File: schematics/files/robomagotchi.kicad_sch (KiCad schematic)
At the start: 26 parts, among them M1 Servo Motor, U1 SPI TFT DISPLAY (ILI9341), U2 I2C OLED Display (SSD1306), U3 Ultrasonic Proximity Sensor (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, U4 Temp Sensor (DHT11), U5 IR Receiver (VS18838B)

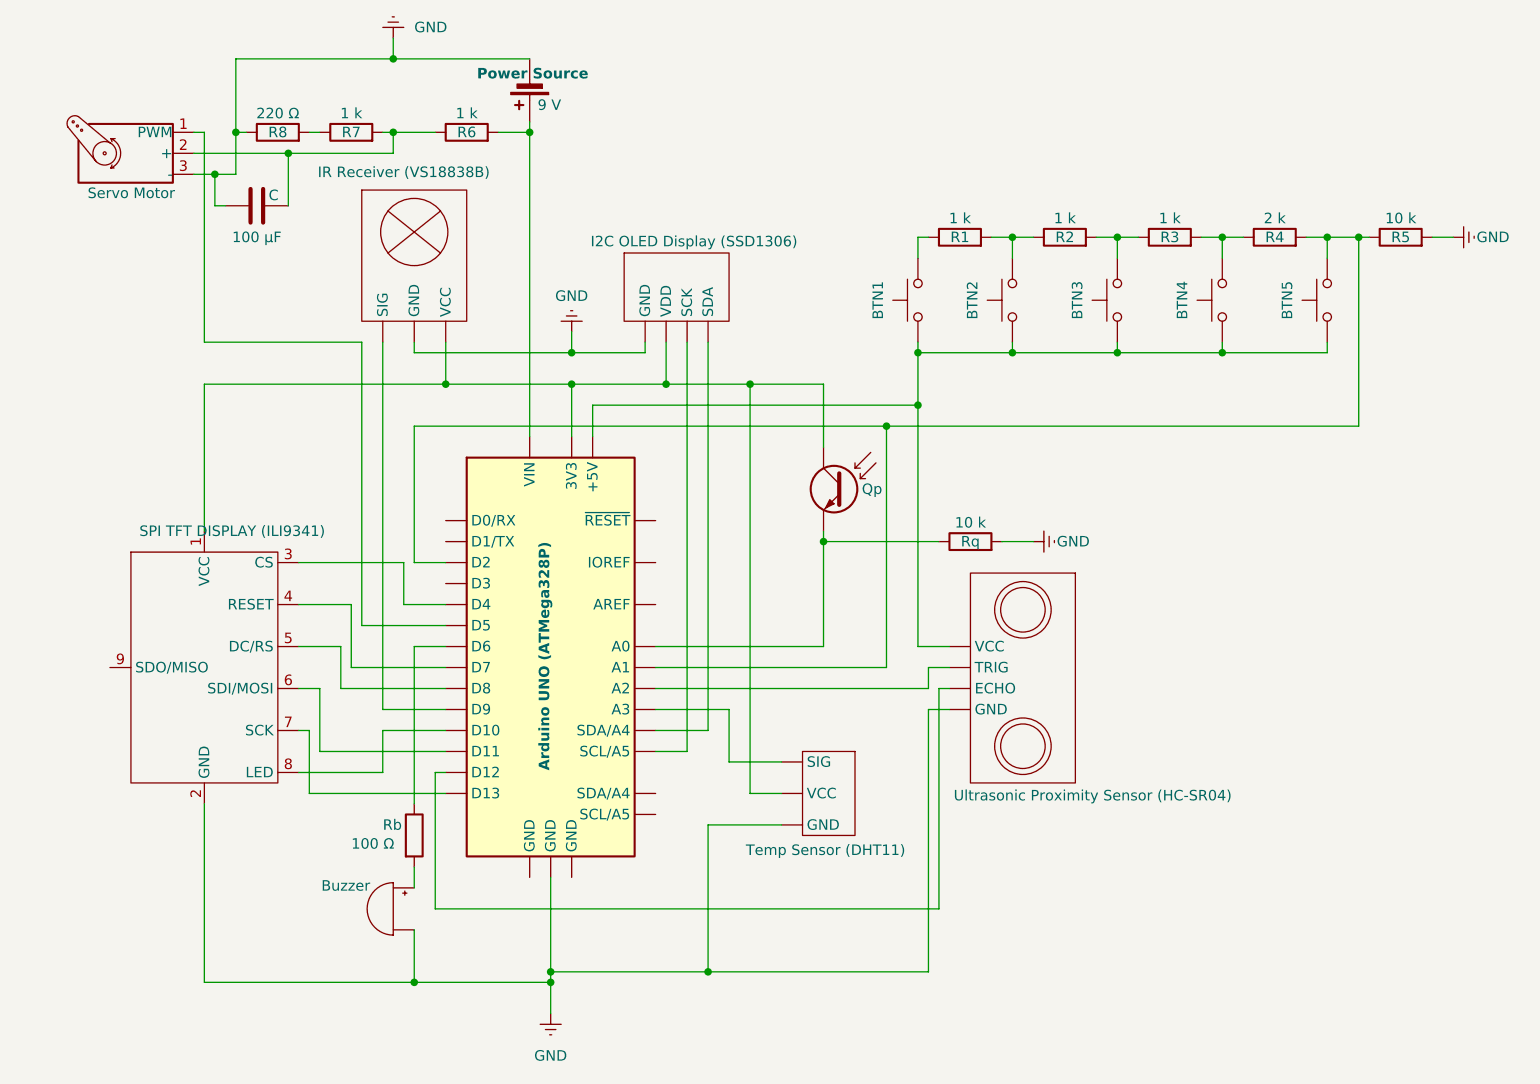
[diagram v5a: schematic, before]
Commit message: Replaced display. Changed resistor ladder.
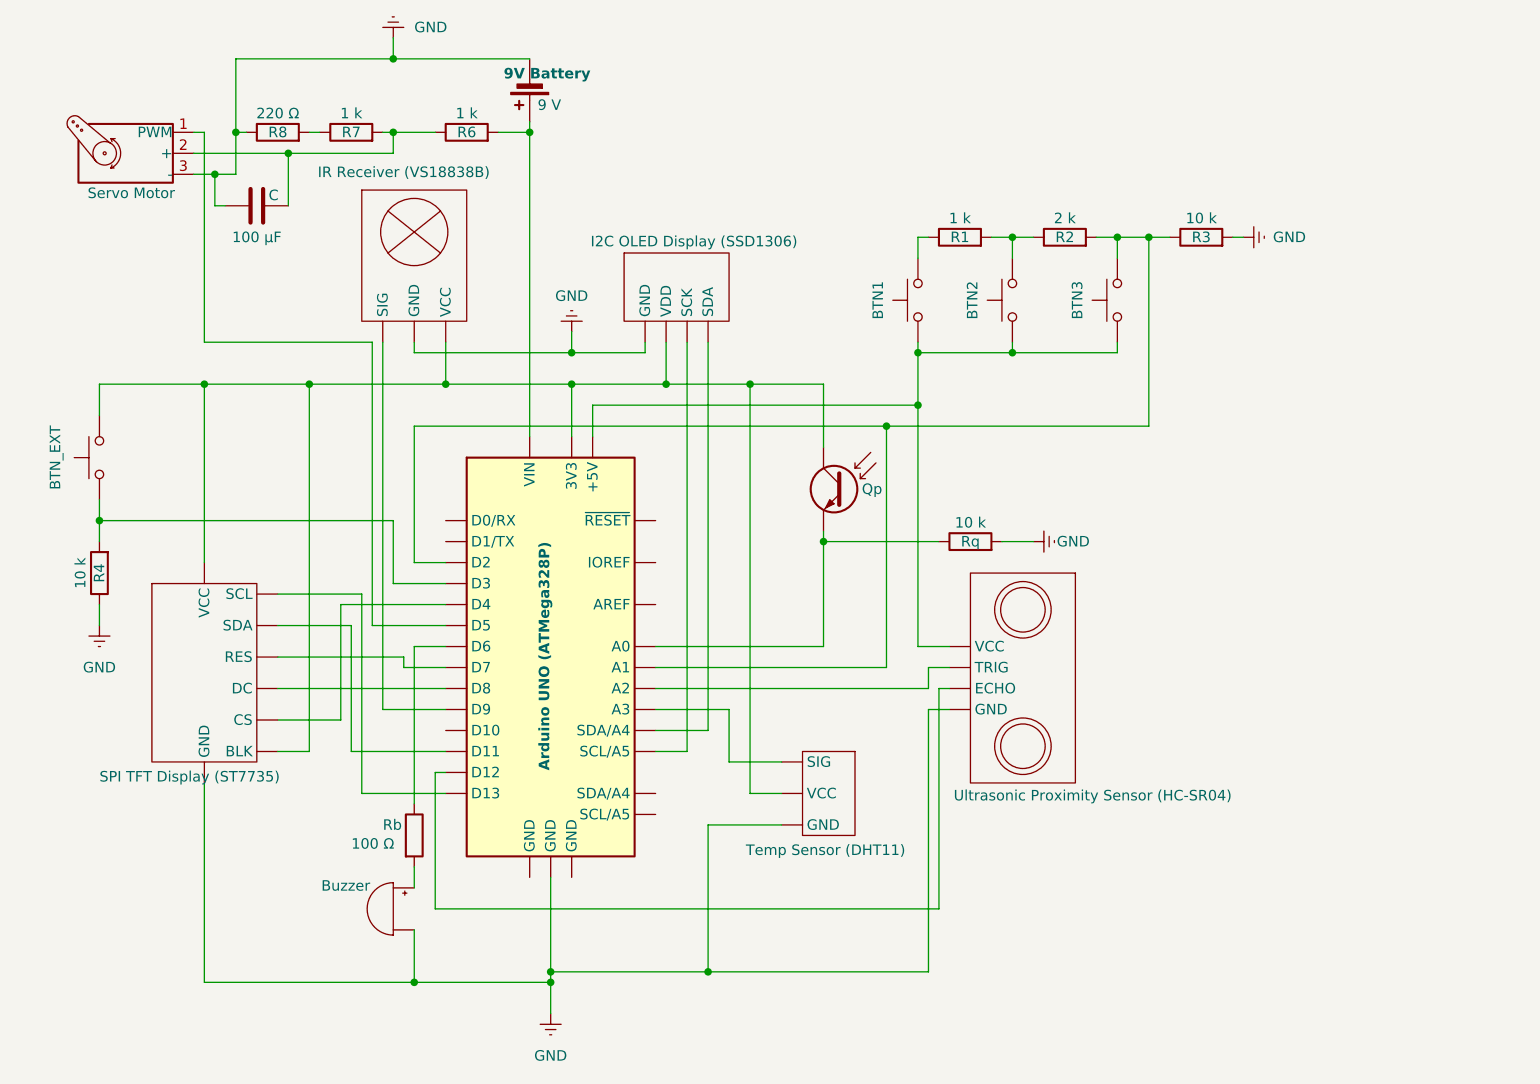
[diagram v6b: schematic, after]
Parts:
- removed BTN5: SW_Push, symbol Switch:SW_Push
- removed R3: 1 k, symbol Device:R
- removed U1: SPI TFT DISPLAY (ILI9341), symbol A_LAPTOP_LIB:ILI9341_SPI_TFT
- added U1: SPI TFT Display (ST7735), symbol A_LAPTOP_LIB:ST7735_SPI_TFT_Display
- R2: value 1 k -> 2 k
- R4: value 2 k -> 10 k
- renumbered BTN4 to BTN_EXT, R5 to R3
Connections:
- net GND: now also R4.1, U1.1 (GND)
- net at BTN3.2, R2.2: now also A2.10 (A1), A2.17 (D2), R3.1
- net at BTN_EXT.2: now also A2.4 (3V3), Qp.1 (C), U2. (VDD), U4. (VCC), U5. (VCC), U1.2 (VCC), U1.8 (BLK); no longer R4.1
- net at A2.5 (+5V), BTN1.1, BTN2.1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: no longer BTN_EXT.1
- net at A2.19 (D4): now also U1.7 (CS)
- net at A2.22 (D7): now also U1.5 (RES)
- net at A2.23 (D8): now also U1.6 (DC)
- net at A2.26 (D11): now also U1.4 (SDA)
- net at A2.28 (D13): now also U1.3 (SCL)
- net at A2.18 (D3): now also BTN_EXT.1, R4.2
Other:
- moved on the sheet: BTN_EXT, R3

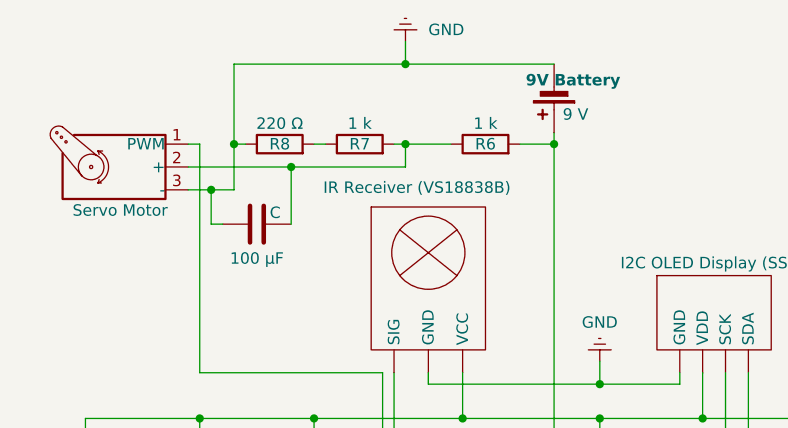
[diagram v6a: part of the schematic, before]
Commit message: Fixed resistor numerotation error.
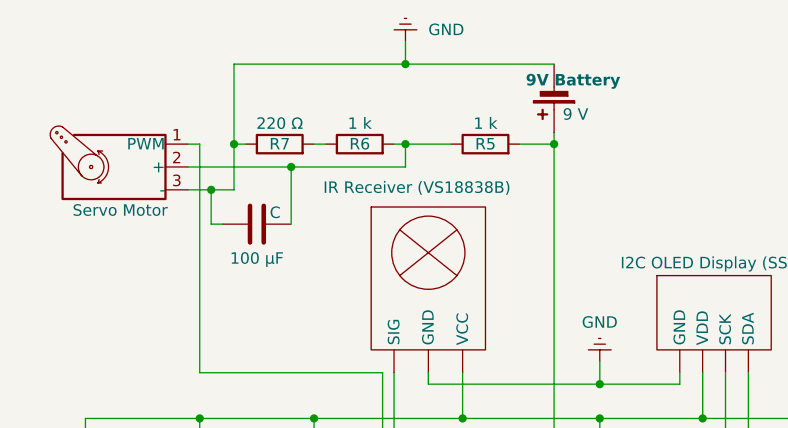
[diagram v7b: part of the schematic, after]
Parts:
- renumbered R6 to R5, R7 to R6, R8 to R7
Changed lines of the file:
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@@
 		(on_board yes)
 		(dnp no)
-		(property "Reference" "R6"
+		(property "Reference" "R5"
 			(at 120.65 44.45 90)
 			(effects
@@
 			(project "robomagotchi"
 				(path "/564f43e2-925d-4726-ad2e-2e1f480b3347"
-					(reference "R6")
+					(reference "R5")
 					(unit 1)
 				)
@@
 		(on_board yes)
 		(dnp no)
-		(property "Reference" "R7"
+		(property "Reference" "R6"
 			(at 106.68 44.45 90)
 			(effects
@@
 			(project "robomagotchi"
 				(path "/564f43e2-925d-4726-ad2e-2e1f480b3347"
-					(reference "R7")
+					(reference "R6")
 					(unit 1)
 				)
@@
 		(on_board yes)
 		(dnp no)
-		(property "Reference" "R8"
+		(property "Reference" "R7"
 			(at 97.79 44.45 90)
 			(effects
@@
 			(project "robomagotchi"
 				(path "/564f43e2-925d-4726-ad2e-2e1f480b3347"
-					(reference "R8")
-					(unit 1)
-				)
+					(reference "R7")
+					(unit 1)
+				)

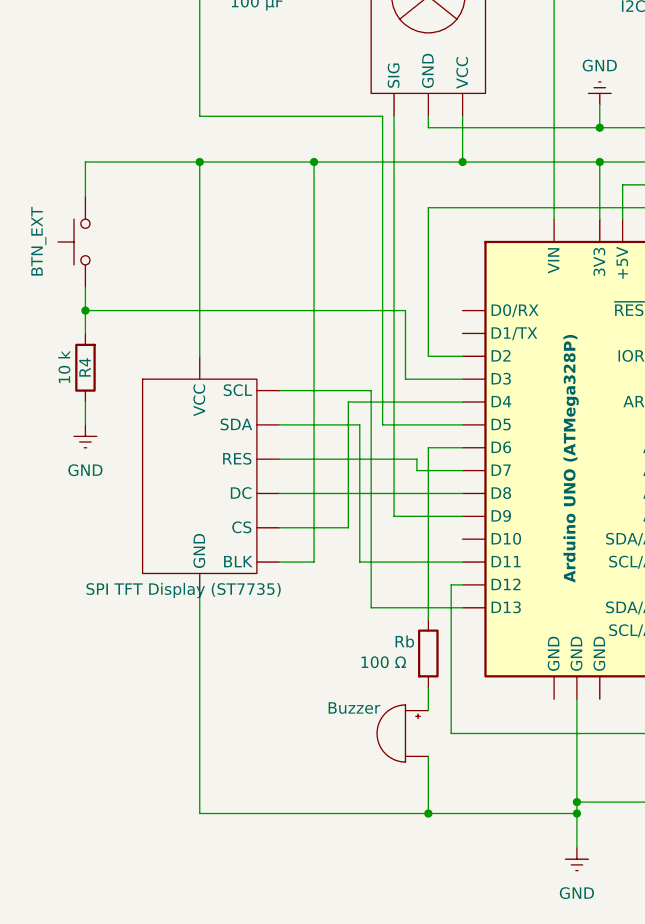
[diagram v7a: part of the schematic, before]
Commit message: Added init funcs for most components
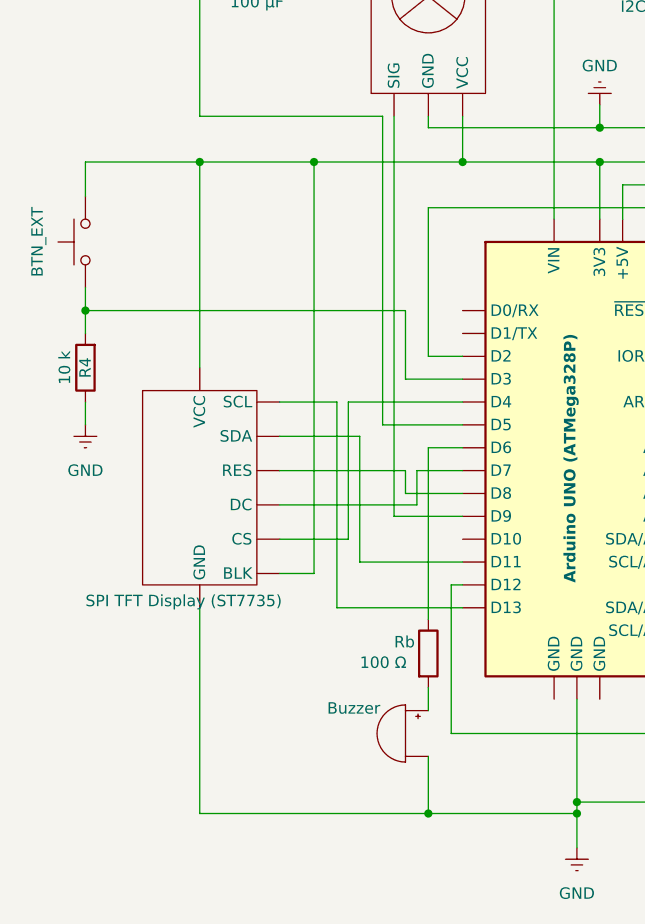
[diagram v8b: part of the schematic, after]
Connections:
- net at U1.5 (RES): now also A2.23 (D8); no longer A2.22 (D7)
- net at U1.6 (DC): now also A2.22 (D7); no longer A2.23 (D8)
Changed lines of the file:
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@@
 		(title "Robomagotchi Electronic Circuit")
 		(date "2025-01-07")
-		(rev "3.1")
+		(rev "3.1.1")
 		(company "Author: Adrian-Mihael Fota")
 		(comment 1 "University of Bucharest")
@@
 	(wire
 		(pts
+			(xy 113.03 109.22) (xy 118.11 109.22)
+		)
+		(stroke
+			(width 0)
+			(type default)
+		)
+	)
+	(wire
+		(pts
 			(xy 135.89 77.47) (xy 175.26 77.47)
 		)
@@
 	(wire
 		(pts
-			(xy 97.79 111.76) (xy 118.11 111.76)
-		)
-		(stroke
-			(width 0)
-			(type default)
-		)
-	)
-	(wire
-		(pts
-			(xy 106.68 104.14) (xy 106.68 119.38)
+			(xy 111.76 109.22) (xy 111.76 111.76)
+		)
+		(stroke
+			(width 0)
+			(type default)
+		)
+	)
+	(wire
+		(pts
+			(xy 106.68 105.41) (xy 106.68 119.38)
 		)
 		(stroke
@@
 	(wire
 		(pts
+			(xy 104.14 124.46) (xy 118.11 124.46)
+		)
+		(stroke
+			(width 0)
+			(type default)
+		)
+	)
+	(wire
+		(pts
 			(xy 114.3 69.85) (xy 114.3 71.12)
 		)
@@
 	(wire
 		(pts
-			(xy 88.9 123.19) (xy 88.9 147.32)
+			(xy 88.9 124.46) (xy 88.9 147.32)
 		)
 		(stroke
@@
 	(wire
 		(pts
+			(xy 111.76 111.76) (xy 118.11 111.76)
+		)
+		(stroke
+			(width 0)
+			(type default)
+		)
+	)
+	(wire
+		(pts
 			(xy 111.76 35.56) (xy 128.27 35.56)
 		)
@@
 	(wire
 		(pts
-			(xy 107.95 100.33) (xy 107.95 124.46)
-		)
-		(stroke
-			(width 0)
-			(type default)
-		)
-	)
-	(wire
-		(pts
 			(xy 171.45 109.22) (xy 171.45 80.01)
 		)
@@
 	(wire
 		(pts
+			(xy 97.79 113.03) (xy 113.03 113.03)
+		)
+		(stroke
+			(width 0)
+			(type default)
+		)
+	)
+	(wire
+		(pts
 			(xy 116.84 138.43) (xy 177.8 138.43)
 		)
@@
 	(wire
 		(pts
-			(xy 107.95 124.46) (xy 118.11 124.46)
-		)
-		(stroke
-			(width 0)
-			(type default)
-		)
-	)
-	(wire
-		(pts
 			(xy 110.49 44.45) (xy 111.76 44.45)
 		)
@@
 	(wire
 		(pts
-			(xy 97.79 104.14) (xy 106.68 104.14)
+			(xy 97.79 105.41) (xy 106.68 105.41)
 		)
 		(stroke
@@
 	(wire
 		(pts
+			(xy 113.03 113.03) (xy 113.03 109.22)
+		)
+		(stroke
+			(width 0)
+			(type default)
+		)
+	)
+	(wire
+		(pts
 			(xy 175.26 106.68) (xy 179.07 106.68)
 		)
@@
 	(wire
 		(pts
-			(xy 88.9 96.52) (xy 88.9 74.93)
+			(xy 88.9 97.79) (xy 88.9 74.93)
 		)
 		(stroke
@@
 	(wire
 		(pts
-			(xy 113.03 109.22) (xy 118.11 109.22)
-		)
-		(stroke
-			(width 0)
-			(type default)
-		)
-	)
-	(wire
-		(pts
 			(xy 88.9 69.85) (xy 88.9 44.45)
 		)
@@
 	(wire
 		(pts
-			(xy 101.6 74.93) (xy 101.6 119.38)
+			(xy 101.6 74.93) (xy 101.6 120.65)
 		)
 		(stroke
@@
 	(wire
 		(pts
-			(xy 97.79 119.38) (xy 101.6 119.38)
+			(xy 97.79 120.65) (xy 101.6 120.65)
 		)
 		(stroke
@@
 	(wire
 		(pts
-			(xy 105.41 115.57) (xy 105.41 101.6)
+			(xy 105.41 116.84) (xy 105.41 101.6)
+		)
+		(stroke
+			(width 0)
+			(type default)
+		)
+	)
+	(wire
+		(pts
+			(xy 97.79 101.6) (xy 104.14 101.6)
 		)
 		(stroke
@@
 	(wire
 		(pts
+			(xy 97.79 109.22) (xy 111.76 109.22)
+		)
+		(stroke
+			(width 0)
+			(type default)
+		)
+	)
+	(wire
+		(pts
 			(xy 185.42 93.98) (xy 189.23 93.98)
 		)
@@
 	(wire
 		(pts
+			(xy 104.14 101.6) (xy 104.14 124.46)
+		)
+		(stroke
+			(width 0)
+			(type default)
+		)
+	)
+	(wire
+		(pts
 			(xy 144.78 74.93) (xy 154.94 74.93)
 		)
@@
 	(wire
 		(pts
-			(xy 113.03 107.95) (xy 113.03 109.22)
-		)
-		(stroke
-			(width 0)
-			(type default)
-		)
-	)
-	(wire
-		(pts
-			(xy 97.79 107.95) (xy 113.03 107.95)
-		)
-		(stroke
-			(width 0)
-			(type default)
-		)
-	)
-	(wire
-		(pts
-			(xy 97.79 115.57) (xy 105.41 115.57)
+			(xy 97.79 116.84) (xy 105.41 116.84)
 		)
 		(stroke
@@
 		(pts
 			(xy 88.9 74.93) (xy 101.6 74.93)
-		)
-		(stroke
-			(width 0)
-			(type default)
-		)
-	)
-	(wire
-		(pts
-			(xy 97.79 100.33) (xy 107.95 100.33)
 		)
 		(stroke
@@
 	(symbol
 		(lib_id "A_LAPTOP_LIB:ST7735_SPI_TFT_Display")
-		(at 88.9 109.22 0)
+		(at 88.9 110.49 0)
 		(unit 1)
 		(exclude_from_sim no)
@@
 		(dnp no)
 		(property "Reference" "U1"
-			(at 81.28 109.2199 0)
+			(at 81.28 110.4899 0)
 			(effects
 				(font
@@
 		)
 		(property "Value" "SPI TFT Display (ST7735)"
-			(at 98.044 122.428 0)
+			(at 98.044 123.698 0)
 			(effects
 				(font
@@
 		)
 		(property "Footprint" ""
-			(at 88.9 109.22 0)
+			(at 88.9 110.49 0)
 			(effects
 				(font
@@
 		)
 		(property "Datasheet" ""
-			(at 88.9 109.22 0)
+			(at 88.9 110.49 0)
 			(effects
 				(font
@@
 		)
 		(property "Description" ""
-			(at 88.9 109.22 0)
-			(effects
-				(font
+			(at 88.9 110.49 0)
+			(effects
+				(font
